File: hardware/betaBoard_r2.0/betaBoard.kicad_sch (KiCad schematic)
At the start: 45 parts, among them J1 DNP, J2 AMPHENOL_10103592-0001LF, J3 DNP, J4 DNP, J5 DNP, J6 DNP, U1 AMS1117-3.3_SOT223

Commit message: main r2.0 design done
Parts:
- removed C42: 10u, Capacitor_SMD:C_1206_3216Metric, symbol Device:C
- removed D10, D11, D14, D6, D7: BPW34-SMD, betaBoard:Osram_BPW34S-SMD_hole, symbol Sensor_Optical:BPW34-SMD
- removed D12, D16, D4, D8: DNP, OptoDevice:Osram_BPW34S-SMD, symbol Sensor_Optical:BPW34-SMD
- removed D17, D18, D24, D25: 1N5819WS, Diode_SMD:D_SOD-323, symbol Diode:1N5819WS
- removed J1: DNP, betaBoard:PinHeader_1x02_P2.54mm_castellation, symbol Connector:Conn_01x02_Male
- removed J3: DNP, Connector_PinSocket_2.54mm:PinSocket_1x02_P2.54mm_Vertical, symbol Connector:Conn_01x02_Female
- removed JP1: DNP, Jumper:SolderJumper-2_P1.3mm_Bridged2Bar_Pad1.0x1.5mm, symbol Jumper:SolderJumper_2_Bridged
- added C22: 100u, Capacitor_SMD:C_1206_3216Metric, symbol Device:C
- added H7, H8, H9: M3 Hole, MountingHole:MountingHole_2.7mm_M2.5_DIN965_Pad, symbol Mechanical:MountingHole_Pad
- added R29, R30, R31, R32: 10k, Resistor_SMD:R_0603_1608Metric, symbol Device:R
- added R33: 4R7, Resistor_SMD:R_0603_1608Metric, symbol Device:R
- C1: value 10u -> 100u
- D15, D2, D3: value BPW34-SMD -> DNP; footprint betaBoard:Osram_BPW34S-SMD_hole -> OptoDevice:Osram_BPW34S-SMD
- R2, R3, R4, R5: value 1k -> 10k
- R45: value 0 -> DNP
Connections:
- net LDO_IN is gone; now on net 5V_USB: C1.1, U1.3 (VI)
- net particle_sensor_array2/Diodes is gone; now on net particle_sensor_array1/Diodes: D2.1 (K)
- net 5V_USB: now also R33.2
- net GND: now also C22.2, H7.1, H8.1, H9.1
- net MCU/GP10: now also R5.1; no longer R2.1
- net MCU/GP11: now also R4.1; no longer R3.1
- net MCU/GP12: now also R3.1; no longer R4.1
- net MCU/GP13: now also R2.1; no longer R5.1
- net MCU/SWD_CLK: now also R30.1; no longer J5.1 (Pin_1)
- net MCU/SWD_SIO: now also R29.1; no longer J5.3 (Pin_3)
- net MCU/UART0_RX: now also R32.1; no longer J4.2 (Pin_2)
- net MCU/UART0_TX: now also R31.1; no longer J4.3 (Pin_3)
- net VCC: now also C22.1, R33.1
- net particle_sensor_array1/Diodes: now also D3.1 (K)
- net particle_sensor_array3/Diodes renamed Frontend Alpha/Diodes
- net Frontend Alpha/Diodes: no longer D3.1 (K)
- new net: J4.2 (Pin_2), R32.2
- new net: J4.3 (Pin_3), R31.2
- new net: J5.1 (Pin_1), R30.2
- new net: J5.3 (Pin_3), R29.2
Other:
- removed sheet particle_sensor_array
- removed sheet particle_sensor_array2
- removed sheet particle_sensor_array3
- added sheet Frontend Alpha (frontend_alpha.kicad_sch)
- sheet MCU ports: added GP23; removed none
- sheet particle_sensor_array1 ports: added out_dc, out_low_gain; removed none
- note added: "3V3 for analog components"
- note added: "Analog 5V supply"
- note added: "Optional components to connect USB shield"
- note removed: "12 V max"
- note removed: "Alternative Power input"
- note removed: "Alternative diode input"
- moved on the sheet: C1, C2, C43, D1, D13, D5, D9, H1, H2, H3, H4, H5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

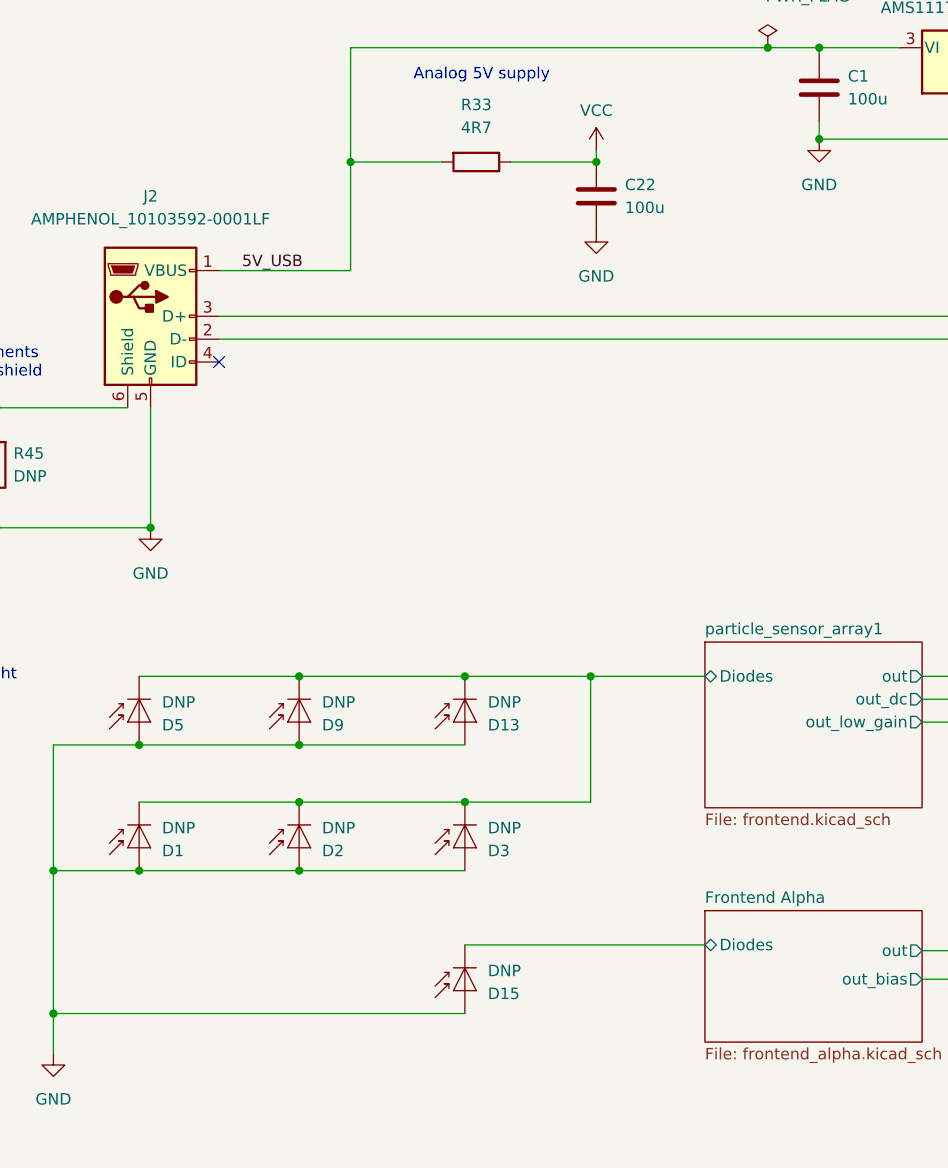
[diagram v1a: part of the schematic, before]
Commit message: hardware: updated kicad version
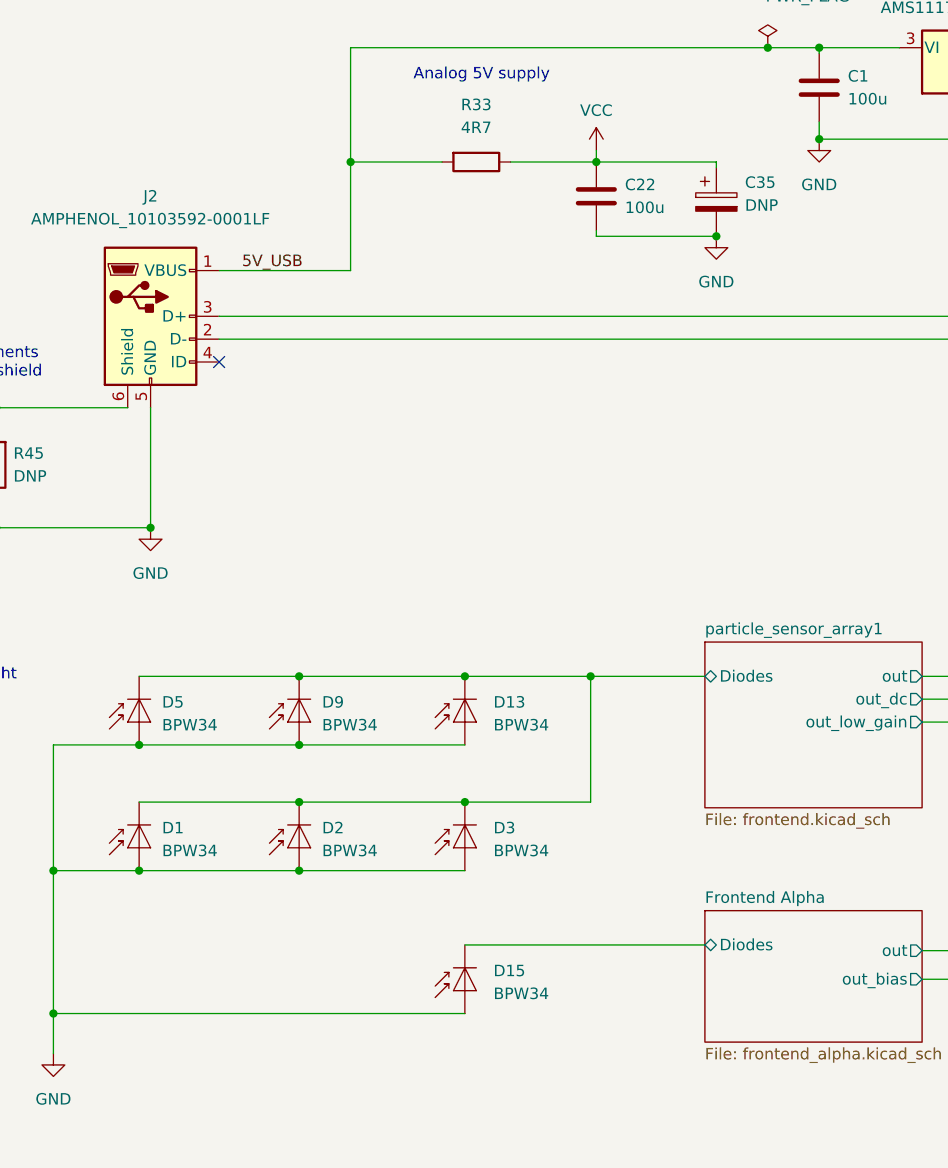
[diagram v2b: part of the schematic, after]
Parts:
- added C35: DNP, Capacitor_THT:CP_Radial_D10.0mm_P5.00mm, symbol Device:C_Polarized
- D1, D13, D15, D2, D3, D5, D9: value DNP -> BPW34
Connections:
- net GND: now also C35.2
- net VCC: now also C35.1
